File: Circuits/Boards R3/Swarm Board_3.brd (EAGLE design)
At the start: 82.1 x 63.5 mm, 147 parts, among them CON1 ISP(2X3), CON2 MAIN_CONNECTOR_14SMD, CON4 HEADER_3X1, CON5 HEADER_3X1, CON7 MAIN_CONNECTOR_8, M1 VIBMOTOR, T1 TEFT4300, T10 TEFT4300, T11 NPN2N2222, T12 SI2333DS-T1, T13 NPN2N2222, T14 NPN2N2222, T15 NPN2N2222, T16 NPN2N2222, T17 NPN2N2222, T18 NPN2N2222, T19 IRLML6244TR, T2 TEFT4300, T20 IRLML6244TR, T21 IRLML6244TR, T22 IRLML6244TR, T23 IRLML6244TR, T3 NPN2N2222, T4 TEFT4300, T5 TEFT4300, T6 TEFT4300, T7 TEFT4300, T8 TEFT4300, T9 TEFT4300, U1 ATMEGA324P, U2 MCP73833, U3 ATMEGA1281, U4 MCP9700A, U5 AH182, U6 AH182, U7 QRE1113, U8 QRE1113

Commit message: more routing
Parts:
- removed U1: ATMEGA324P, DigitalIC:TQFP44
- C17: device Passive:CAP-PTH-SMALL-POL -> Passive:0805
- C9: value 1uf -> 10uf; device Passive:0603 -> Passive:0805
- CON2: value MAIN_CONNECTOR_14SMD -> MAIN_CONNECTOR_14
- moved LED15 214.5 mm to (97.8, 50.8)
- moved R6 210.5 mm to (42.9, 57.2), turned to 270 degrees
- moved R25 210.3 mm to (55.1, 44.7), turned to 225 degrees
- moved R56 210.2 mm to (94.8, 51.1)
- moved LED14 209.4 mm to (97.8, 48.6)
- moved R55 205.2 mm to (94.8, 48.9)
- moved R61 205.1 mm to (18.8, 54.9), turned to 315 degrees
- moved LED12 204.6 mm to (97.8, 46.5)
- moved R54 200.4 mm to (94.8, 46.8)
- moved LED11 196.9 mm to (97.7, 44.1)
- moved R53 196.9 mm to (94.8, 44.1)
- moved R34 196.4 mm to (53.3, 24.4), turned to 180 degrees
- moved R62 192.6 mm to (44.2, 12.4), turned to 225 degrees
- moved R60 184.3 mm to (15.9, 33.5), turned to 270 degrees
- moved R52 170.9 mm to (27.9, 10.8), turned to 90 degrees
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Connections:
- removed net IRBUMPER: U1.34
- new net N$60: U3.P$35
- new net N$61: U3.P$36
- new net N$62: U3.P$37
- new net N$63: U3.P$38
- new net N$64: U3.P$39
- new net N$65: U3.P$40
- new net N$66: U3.P$41
- new net N$67: U3.P$42
- new net N$68: U3.P$29
- new net N$69: U3.P$30
- new net N$70: U3.P$31
- new net N$71: U3.P$32
- new net N$72: U3.P$61
- new net N$73: U3.P$60
- new net N$74: U3.P$59
- new net N$75: U3.P$58
- new net N$76: U3.P$57
- new net N$77: U3.P$56
- new net N$78: U3.P$55
- new net N$79: U3.P$54
- new net N$80: U3.P$33
- new net N$81: U3.P$34
- new net N$82: U3.P$43
- new net N$83: U3.P$18
- new net N$84: U3.P$19
- new net N$85: U3.P$51
- new net N$86: U3.P$50
- new net N$87: U3.P$49
- new net N$88: U3.P$48
- new net N$89: U3.P$47
- new net N$90: U3.P$46
- new net N$91: U3.P$45
- new net N$92: U3.P$44
- net +3V: now also C17.1; no longer C17.+
- net AIN1: no longer U1.14
- net AIN2: no longer U1.19
- net APWM: no longer U1.16
- net BIN1: no longer U1.12
- net BIN2: no longer U1.11
- net BPWM: no longer U1.15
- net BUZZER: no longer U1.44
- net CHGDETECT: no longer U1.40
- net CHGSTATUS: no longer U1.41
- net DISTANCELED: no longer U1.31
- net DISTANCERECEIVE: no longer U1.30
- net GND: now also C17.2; no longer C17.-
- net IRENABLE: no longer U1.33
- net LED1: no longer U1.42
- net LED2: no longer U1.43
- net LIGHTSENSE: no longer U1.32
- net LINESENSE1: no longer U1.36
- net LINESENSE2: no longer U1.35
- net RX1: no longer U1.21
- net RX2: no longer U1.22
- net RX3: no longer U1.23
- net RX4: no longer U1.24
- net RX5: no longer U1.25
- net RX6: no longer U1.26
- net STBY: no longer U1.13
- net TRANSMITLEDS: no longer U1.20
- net VBATSENSE: no longer U1.37
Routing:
- net N$10: track 1.10 -> 206.8 mm, vias 0 -> 7
- net GND: track 51.2 -> 72.6 mm, vias 9 -> 18
- net +VRAW: track 16.8 -> 10.2 mm, vias 3 -> 2
- net +3V: track 33.1 -> 26.8 mm
- net N$27: track 0.00 -> 5.97 mm
- net N$26: track 0.46 -> 4.31 mm
- net VBATSENSE: track 2.98 -> 5.20 mm
- net RX1: track 0.00 -> 2.04 mm
- net N$9: track 4.27 -> 6.25 mm
- net N$20: track 0.00 -> 1.98 mm
- net AIN1: track 9.07 -> 11.0 mm
- net AIN2: track 9.74 -> 11.5 mm
- net APWM: track 10.4 -> 12.1 mm
- net RX6: track 2.10 -> 3.61 mm
- net STBY: track 7.24 -> 8.52 mm
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- added copper zone on layer 1, net +3V
- removed copper zone on layer 1, net +VRAW

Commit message: more routing
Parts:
- added W1, W2, W3: WHISKER, Mechanical:WHISKER
- moved R57 172.3 mm to (50.8, 18.9), turned to 180 degrees
- moved T23 171.7 mm to (53.0, 20.9)
- moved R58 170.7 mm to (45.7, 24.0)
- moved M1 159.4 mm to (42.4, 16.8), turned to 180 degrees
- moved C16 158.1 mm to (43.9, 17.9)
- moved T12 65.6 mm to (18.7, 10.8), turned to 270 degrees
- moved LED15 63.5 mm to (36.2, 35.4), turned to 270 degrees
- moved C4 61.6 mm to (19.7, 13.8)
- moved R7 59.2 mm to (8.89, 23.6)
- moved R56 58.9 mm to (38.1, 35.4), turned to 90 degrees
- moved R55 57.3 mm to (44.2, 22.0)
- moved R54 57.2 mm to (44.2, 20.1)
- moved LED14 57.0 mm to (47.5, 22.0)
- moved LED12 56.8 mm to (47.5, 20.1)
- moved C17 54.6 mm to (18.6, 24.7), turned to 180 degrees
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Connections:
- removed net ????: CON2.12
- removed net N$40: R48.1
- removed net N$41: R49.1
- removed net N$42: R6.2
- removed net N$49: R25.2
- removed net N$50: R34.2
- removed net N$51: R52.2
- removed net N$52: R59.2
- removed net N$53: R60.2
- removed net N$54: R61.2
- removed net N$55: R62.2
- removed net N$56: U3.P$25
- removed net N$57: U3.P$26
- removed net N$60: U3.P$35
- removed net N$61: U3.P$36
- removed net N$62: U3.P$37
- removed net N$63: U3.P$38
- removed net N$64: U3.P$39
- removed net N$65: U3.P$40
- removed net N$66: U3.P$41
- removed net N$67: U3.P$42
- removed net N$68: U3.P$29
- removed net N$72: U3.P$61
- removed net N$73: U3.P$60
- removed net N$74: U3.P$59
- removed net N$75: U3.P$58
- removed net N$76: U3.P$57
- removed net N$77: U3.P$56
- removed net N$78: U3.P$55
- removed net N$79: U3.P$54
- removed net N$81: U3.P$34
- removed net N$85: U3.P$51
- removed net N$86: U3.P$50
- removed net N$87: U3.P$49
- removed net N$88: U3.P$48
- removed net N$89: U3.P$47
- removed net N$90: U3.P$46
- removed net N$91: U3.P$45
- removed net N$92: U3.P$44
- removed net S????: CON7.5
- removed net SLINSENSE2: R33.2, U7.P$4
- net AIN1: now also U3.P$47
- net AIN2: now also U3.P$48
- net BIN1: now also U3.P$45
- net BIN2: now also U3.P$44
- net CHGDETECT: now also U3.P$59
- net CHGSTATUS: now also U3.P$60
- net DISTANCELED: now also U3.P$50
- net DISTANCERECEIVE: now also U3.P$56
- net ENCA: now also U3.P$25
- net ENCB: now also U3.P$26
- net IRENABLE: now also U3.P$42
- net LED1: now also U3.P$39
- net LED2: now also U3.P$38
- net LED3: now also U3.P$37
- net LED5: now also U3.P$34
- net LED6: now also U3.P$35
- net LED7: now also U3.P$49
- net LEFTBUMPER: now also U3.P$40
- net LIGHTSENSE: now also U3.P$55
- net LINESENSE1: now also U3.P$58
- net LINESENSE2: now also U3.P$57
- net MISO: now also R61.2
- net MOSI: now also R6.2
- net PB0: now also R34.2
- net PB4: now also R60.2
- net PB5: now also R59.2
- net PB6: now also R52.2
- net PB7: now also R62.2
- net RIGHTBUMPER: now also U3.P$41
- net S+VSENSE: now also W3.P$1, W3.P$2; no longer R48.2, R49.2
- net SCK: now also R25.2
- net SEN: now also U3.P$4
- net SGND: now also R48.1, R49.1
- net SLEFTBUMPER: now also R49.2, W1.P$1, W1.P$2
- net SLINESENSE2: now also R33.2, U7.P$4
- net SRIGHTBUMPER: now also R48.2, W2.P$1, W2.P$2
- net STBY: now also U3.P$46
- net TEMPSENSE: now also U3.P$54
- net TRANSMITLEDS: now also U3.P$29
- net VBATSENSE: now also U3.P$61
- net VIBE: now also U3.P$36
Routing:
- net ENCB: track 0.00 -> 48.7 mm, vias 0 -> 1
- net +3V: track 26.8 -> 65.1 mm, vias 2 -> 8
- net SRIGHTBUMPER: track 0.00 -> 34.3 mm, vias 0 -> 2
- net GND: track 72.6 -> 105.6 mm, vias 18 -> 28
- net RESET: track 0.00 -> 31.8 mm, vias 0 -> 2
- net ENCA: track 0.00 -> 31.5 mm, vias 0 -> 2
- net SLINESENSE1: track 0.00 -> 29.7 mm, vias 0 -> 2
- net PB7: track 0.00 -> 26.4 mm, vias 0 -> 2
- net +VCHG: track 20.8 -> 45.8 mm, vias 0 -> 1
- net SEN: track 0.00 -> 22.7 mm, vias 0 -> 2
- net BUZZER: track 0.00 -> 22.2 mm, vias 0 -> 2
- net TRANSMITLEDS: track 0.00 -> 19.9 mm
- net PB4: track 0.00 -> 18.9 mm, vias 0 -> 2
- net N$2: track 0.00 -> 17.4 mm
- net PB5: track 0.00 -> 16.2 mm
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- added copper zone on layer 15, net S+VSENSE
- added copper zone on layer 2, net SGND
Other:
- outline, holes or cut-outs redrawn

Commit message: almost there
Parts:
- moved LED11 49.0 mm to (21.6, 28.1), turned to 90 degrees
- moved R53 48.0 mm to (21.6, 25.0), turned to 90 degrees
- moved C5 5.97 mm to (27.1, 45.5)
- moved U4 0.46 mm to (41.1, 34.1)
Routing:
- net MISO: track 10.6 -> 59.0 mm, vias 0 -> 2
- net +VRAW: track 24.0 -> 65.3 mm, vias 3 -> 4
- net +VSENSE: track 27.0 -> 66.3 mm, vias 1 -> 3
- net VBATSENSE: track 4.93 -> 30.3 mm, vias 1 -> 2
- net +VBAT: track 8.32 -> 23.6 mm
- net LINESENSE2: track 0.00 -> 13.1 mm, vias 0 -> 1
- net LINESENSE1: track 0.00 -> 12.2 mm, vias 0 -> 1
- net LED4: track 0.00 -> 4.49 mm
- net RX3: track 1.96 -> 5.89 mm
- net GND: track 105.6 -> 109.4 mm, vias 28 -> 29
- net BUZZER: track 22.2 -> 26.0 mm
- net PB0: track 0.00 -> 3.70 mm, vias 0 -> 1
- net SEN: track 22.7 -> 25.5 mm
- net +3V: track 65.1 -> 66.8 mm
- net N$43: track 0.00 -> 1.61 mm
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
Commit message: schematic at 100%
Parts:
- moved TST1 181.0 mm to (41.8, 26.6)
- moved TST2 174.4 mm to (39.5, 16.8)
- moved R23 0.83 mm to (21.8, 54.8), turned to 90 degrees
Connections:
- removed net N$58: U3.P$8
- removed net N$59: U3.P$9
- removed net N$69: U3.P$30
- removed net N$70: U3.P$31
- removed net N$71: U3.P$32
- removed net N$80: U3.P$33
- removed net N$82: U3.P$43
- removed net N$83: U3.P$18
- removed net N$84: U3.P$19
- net DEBUG1: now also U3.P$43
- net DEBUG2: now also U3.P$33
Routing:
- net SCK: track 10.7 -> 59.9 mm, vias 0 -> 2
- net PB0: track 3.70 -> 33.0 mm, vias 1 -> 2
- net DISTANCELED: track 3.12 -> 20.3 mm
- net +VRAW: track 65.3 -> 81.4 mm
- net MOSI: track 13.5 -> 19.0 mm, vias 0 -> 1
- net DEBUG2: track 0.00 -> 2.60 mm
- net DEBUG1: track 0.00 -> 2.34 mm
- net N$10: track 215.2 -> 214.6 mm
- net MISO: track 59.0 -> 58.5 mm
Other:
- board text removed: "+3V"
- board text removed: "B+"
- board text removed: "B-"
- board text removed: "MA+"
- board text removed: "MA-"
- board text removed: "MB+"
- board text removed: "MB-"
- board text removed: "PA1"
- board text removed: "PA2"
- board text removed: "PA3"
- board text removed: "PA4T"

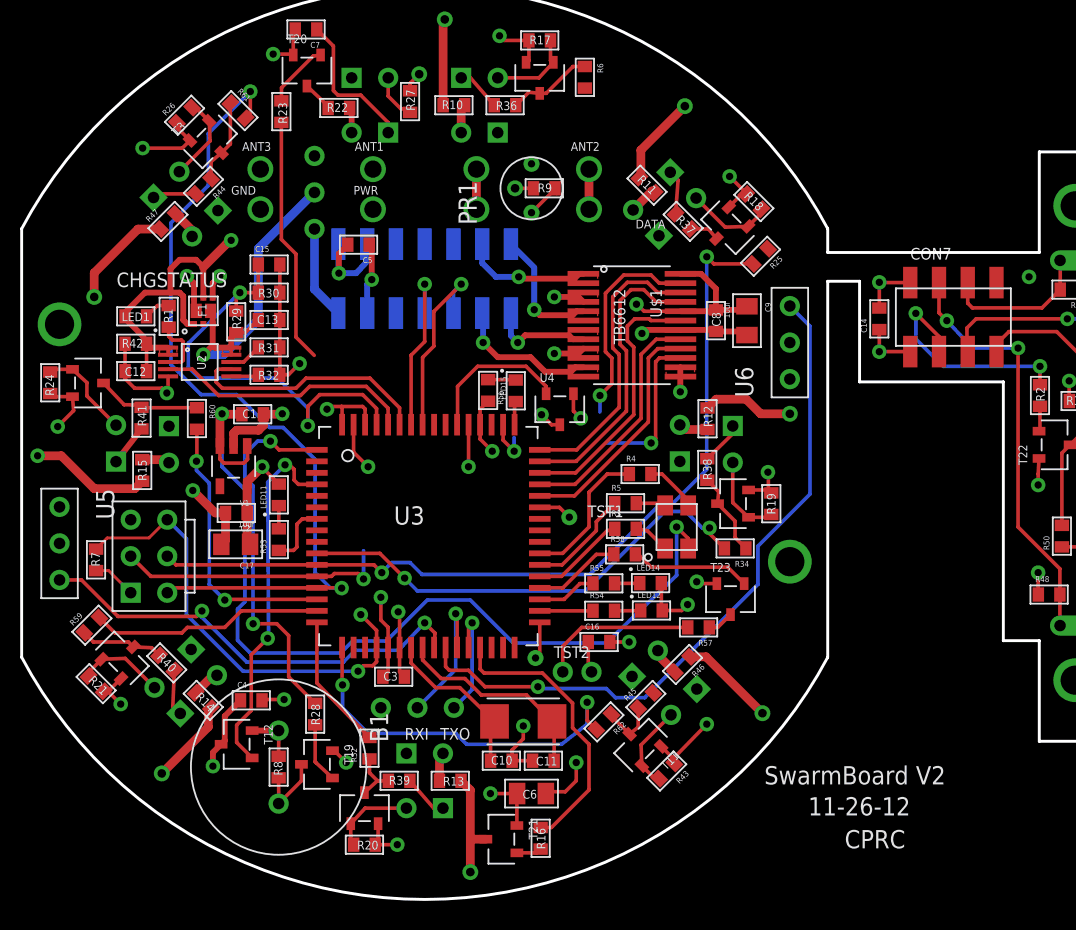
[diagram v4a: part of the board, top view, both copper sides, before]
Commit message: swarm board routing done!
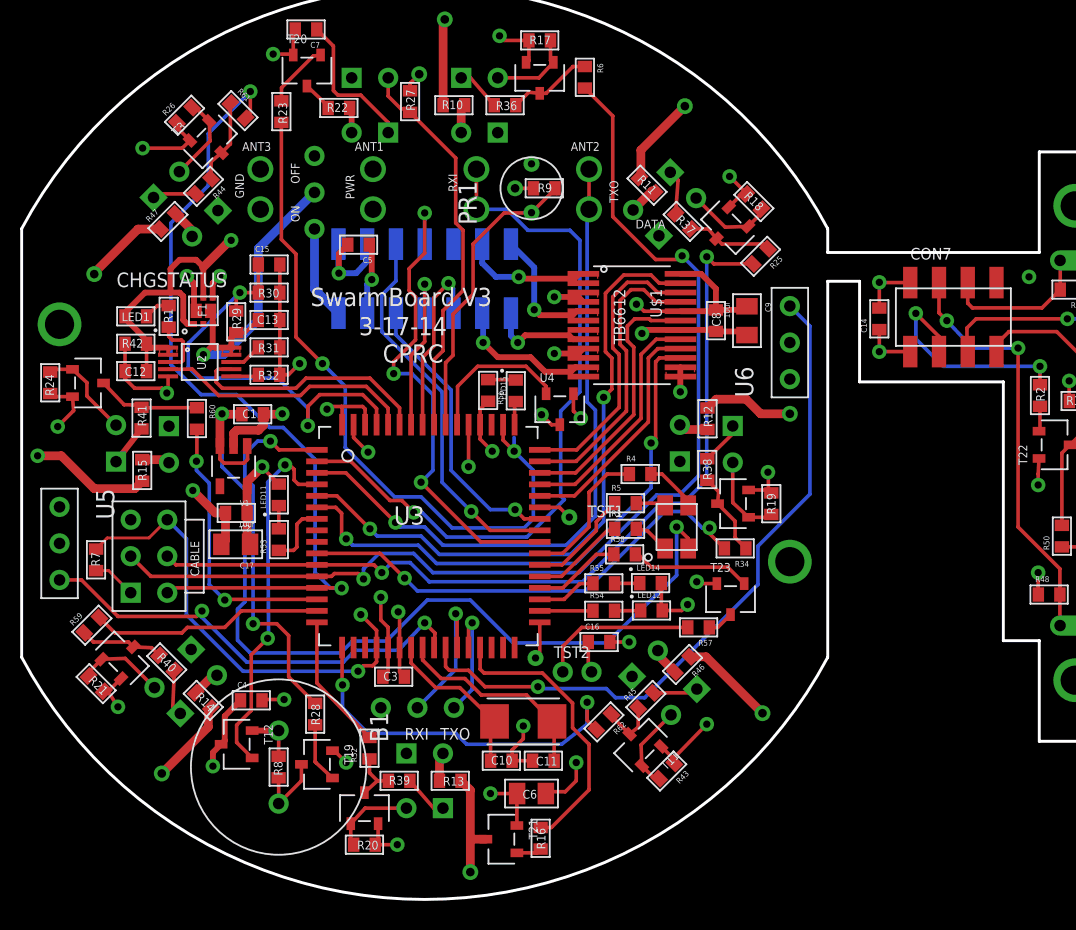
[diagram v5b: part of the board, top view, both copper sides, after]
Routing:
- net MOSI: track 19.0 -> 76.5 mm, vias 1 -> 2
- net CRX: track 2.79 -> 50.0 mm, vias 0 -> 1
- net CTX: track 2.79 -> 46.7 mm, vias 0 -> 1
- net LEFTBUMPER: track 0.00 -> 34.4 mm, vias 0 -> 3
- net APWM: track 14.8 -> 44.9 mm, vias 1 -> 2
- net DISTANCELED: track 20.3 -> 48.5 mm, vias 1 -> 2
- net BPWM: track 10.7 -> 38.6 mm, vias 1 -> 2
- net RIGHTBUMPER: track 0.00 -> 26.9 mm, vias 0 -> 1
- net DISTANCERECEIVE: track 3.40 -> 27.5 mm
- net IRENABLE: track 0.00 -> 20.1 mm, vias 0 -> 1
- net LIGHTSENSE: track 2.74 -> 21.1 mm
- net RX2: track 2.10 -> 5.98 mm
- net +VSENSE: track 66.3 -> 69.4 mm
- net GND: track 109.4 -> 108.4 mm
- net SCK: track 59.9 -> 60.7 mm
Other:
- board text added: "3-17-14"
- board text added: "CABLE"
- board text added: "OFF"
- board text added: "ON"
- board text added: "SwarmBoard V3"
- board text removed: "11-26-12"
- board text removed: "SwarmBoard V2"

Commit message: both boards are routed
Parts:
- flipped CON4 to the top
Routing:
- net +VCHG: track 45.6 -> 37.1 mm
- net GND: track 108.4 -> 114.3 mm
- net N$10: track 214.6 -> 216.7 mm
- net +VSENSE: track 69.4 -> 70.0 mm
- net +3V: track 66.8 -> 67.3 mm
- net SGND: vias 7 -> 6
